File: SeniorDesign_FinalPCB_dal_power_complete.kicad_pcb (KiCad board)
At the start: 2 copper layers, 172.7 x 167.4 mm, 262 parts, among them J1 5000, J10 5000, J11 POWER, J12 AudioJack3, J2 5000, J3 5000, J4 5000, J5 5000, J6 5000, J7 5000, J8 5000, J9 5000, Q1 Si7450DP, Q10 Si7450DP, Q11 Si7450DP, Q12 Si7450DP, Q13 Si7450DP, Q14 Si7450DP, Q15 Si7450DP, Q16 Si7450DP, Q2 Si7450DP, Q3 Si7450DP, Q4 Si7450DP, Q5 Si7450DP, Q6 Si7450DP, Q7 Si7450DP, Q8 Si7450DP, Q9 Si7450DP, U1 Transducer, U10 Transducer, U11 Transducer, U12 Transducer, U13 Transducer, U14 Transducer, U15 Transducer, U16 Transducer, U17 Transducer, U18 Transducer, U19 Transducer, U2 Transducer, U20 Transducer, U21 Transducer, U22 Transducer, U23 Transducer, U24 Transducer, U25 Transducer, U26 Transducer, U27 Transducer, U28 Transducer, U29 Transducer, U3 Transducer, U30 Transducer, U31 Transducer, U32 Transducer, U33 Transducer, U34 Transducer, U35 Transducer, U36 Transducer, U37 Transducer, U38 Transducer, U39 Transducer, U4 Transducer, U40 Transducer, U41 Transducer, U42 Transducer, U43 Transducer, U44 Transducer, U45 Transducer, U46 Transducer, U47 Transducer, U48 Transducer, U49 Transducer, U5 Transducer, U50 Transducer, U51 Transducer, U52 Transducer, U53 Transducer, U54 Transducer, U55 Transducer, U56 Transducer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

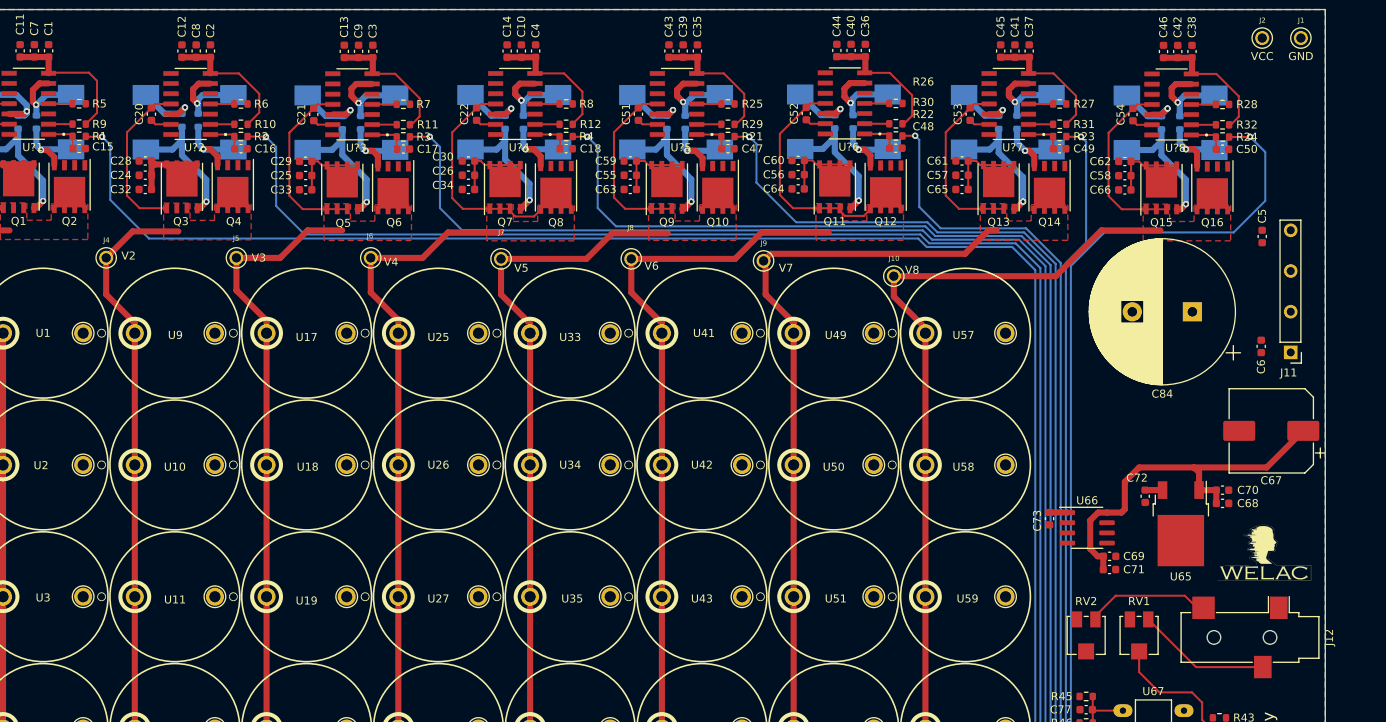
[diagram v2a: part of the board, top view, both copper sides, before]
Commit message: Add 3D Models, Adjust components, Minor changes
- Footprint for 1206 Capacitors is in the footprints folder
- Added a mostly correct size transducer 3D model
- Added the 3D model for the screw terminal
- The above models are in a new folder called SeniorDesign_3DModels
- Fixed some component placements and silkscreens that overlapped
- Added 3D models for all resistors and capacitors of the power circuits
- Fixed the VCC testpoint to be VPP
- Adjusted the Transducer footprint to be 16.3mm in diameter in the event it is deemed necessary to change the spacing of the transducers to make sure they dont interfere with each other
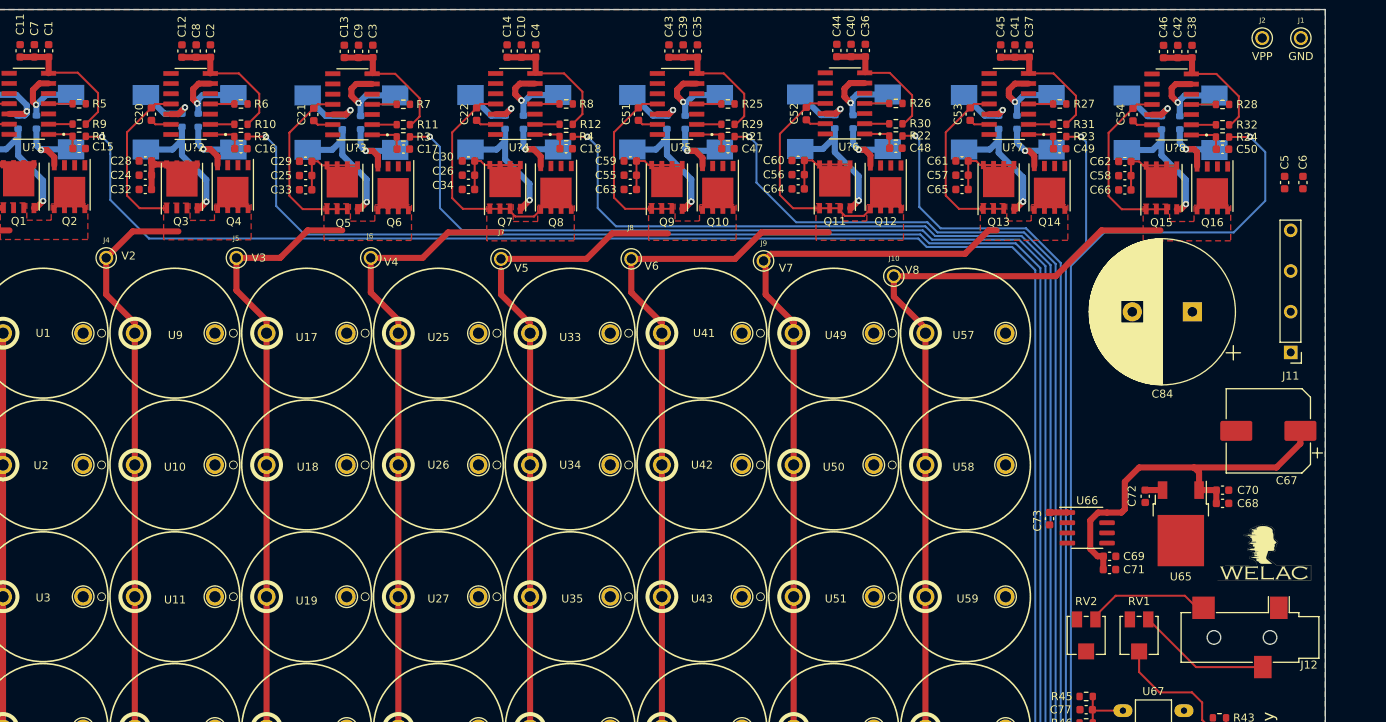
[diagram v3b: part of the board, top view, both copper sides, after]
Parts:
- moved C6 21.1 mm to (472.2, 41.4), turned to -90 degrees
- moved C5 7.29 mm to (469.9, 41.4), turned to -90 degrees
- moved C67 0.37 mm to (467.9, 72.4)
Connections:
- J2 pad 1: VCC -> VPP
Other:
- board text added: "VPP"
- board text removed: "VCC"

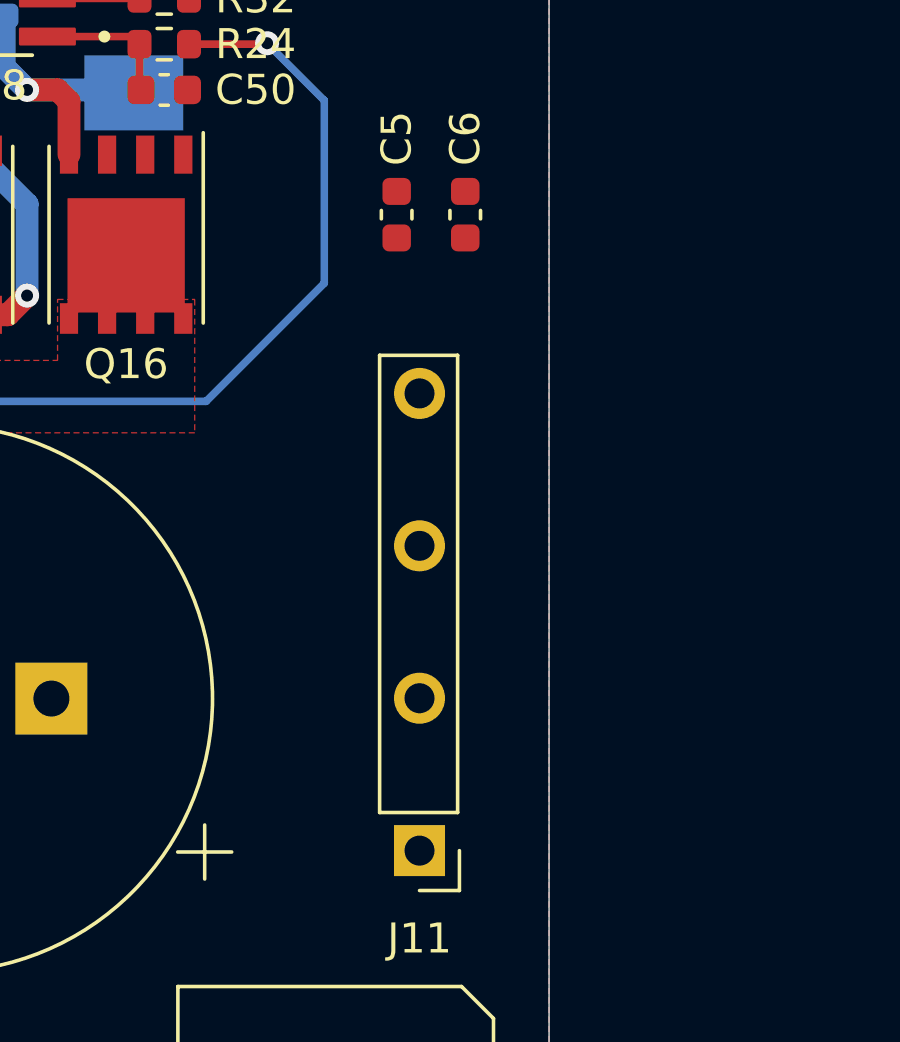
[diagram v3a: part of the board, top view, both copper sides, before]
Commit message: Add missing traces
Added traces on capacitors above the screw terminal
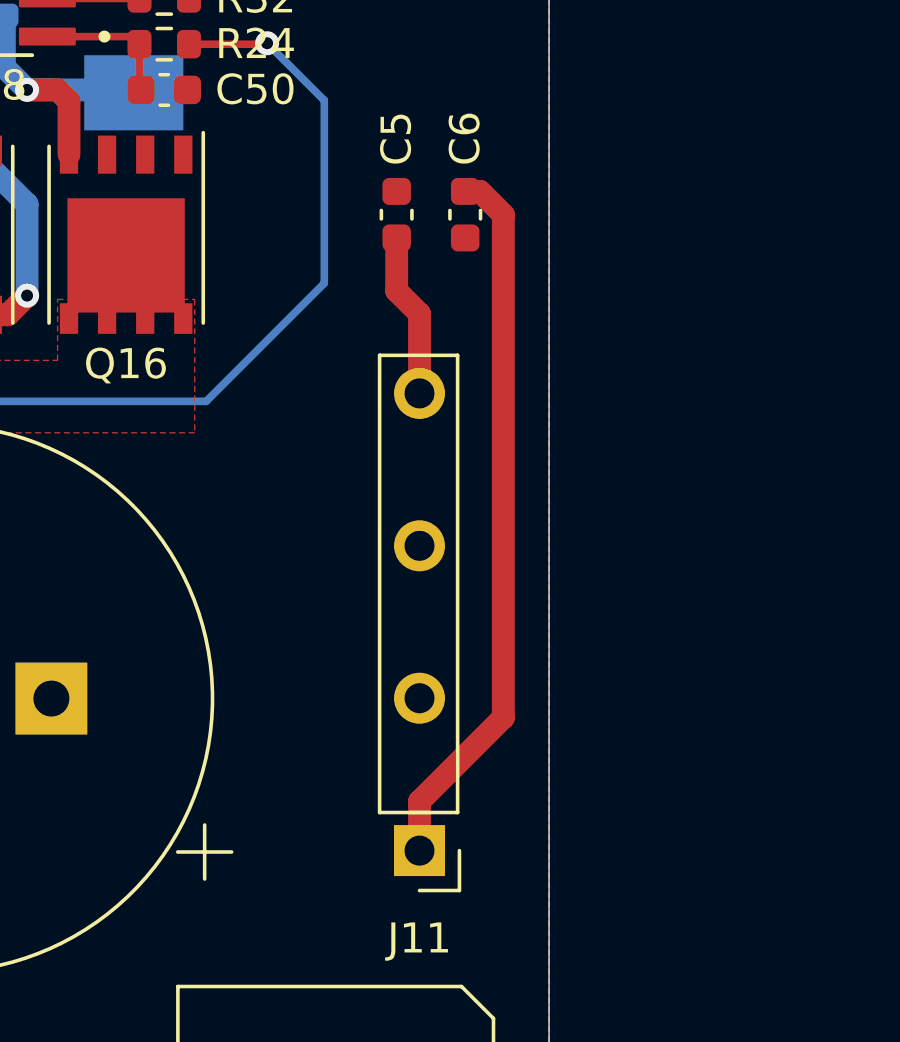
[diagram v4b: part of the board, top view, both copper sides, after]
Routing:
- net +12V: track 183.7 -> 207.6 mm
- net VPP: track 75.6 -> 81.1 mm
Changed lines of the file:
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@@
   (segment (start 396.621 27.699) (end 396.536 27.784) (width 0.25) (layer "F.Cu") (net 2))
   (segment (start 423.418 33.049) (end 423.418 30.509) (width 0.25) (layer "F.Cu") (net 2))
+  (segment (start 470.662 62.6) (end 470.662 60.96) (width 0.762) (layer "F.Cu") (net 2))
   (segment (start 420.624 27.715) (end 417.491 27.715) (width 0.25) (layer "F.Cu") (net 2))
   (segment (start 446.567 88.046) (end 445.643 87.122) (width 0.762) (layer "F.Cu") (net 2))
@@
   (segment (start 339.4005 27.784) (end 335.83 27.784) (width 0.25) (layer "F.Cu") (net 2))
   (segment (start 442.658 34.134) (end 443.865 32.927) (width 0.25) (layer "F.Cu") (net 2))
+  (segment (start 470.662 60.96) (end 473.456 58.166) (width 0.762) (layer "F.Cu") (net 2))
   (segment (start 447.738 82.585) (end 449.545 82.585) (width 0.762) (layer "F.Cu") (net 2))
   (segment (start 468.884 76.962) (end 471.868 73.978) (width 0.762) (layer "F.Cu") (net 2))
   (segment (start 471.868 73.978) (end 471.868 72.39) (width 0.762) (layer "F.Cu") (net 2))
   (segment (start 449.545 82.585) (end 449.961 82.169) (width 0.762) (layer "F.Cu") (net 2))
+  (segment (start 473.456 41.402) (end 472.681 40.627) (width 0.762) (layer "F.Cu") (net 2))
   (segment (start 446.624 82.585) (end 447.738 82.585) (width 0.762) (layer "F.Cu") (net 2))
   (segment (start 422.402 34.065) (end 423.418 33.049) (width 0.25) (layer "F.Cu") (net 2))
@@
   (segment (start 447.269 89.697) (end 447.269 88.059) (width 0.762) (layer "F.Cu") (net 2))
   (segment (start 376.428 27.699) (end 376.343 27.784) (width 0.25) (layer "F.Cu") (net 2))
+  (segment (start 473.456 58.166) (end 473.456 41.402) (width 0.762) (layer "F.Cu") (net 2))
   (segment (start 434.467 25.765) (end 438.023 25.765) (width 0.762) (layer "F.Cu") (net 2))
   (segment (start 315.6515 25.739) (end 315.6515 27.7435) (width 0.762) (layer "F.Cu") (net 2))
@@
   (segment (start 320.2865 34.108) (end 321.818 32.5765) (width 0.254) (layer "F.Cu") (net 2))
   (segment (start 445.643 83.566) (end 446.624 82.585) (width 0.762) (layer "F.Cu") (net 2))
+  (segment (start 472.681 40.627) (end 472.186 40.627) (width 0.762) (layer "F.Cu") (net 2))
   (segment (start 312.0955 25.739) (end 315.6515 25.739) (width 0.762) (layer "F.Cu") (net 2))
   (segment (start 321.818 30.226) (end 319.278 27.686) (width 0.254) (layer "F.Cu") (net 2))
@@
   (segment (start 374.523 39.213) (end 370.713 39.213) (width 0.25) (layer "F.Cu") (net 3))
   (segment (start 436.118 39.213) (end 432.308 39.213) (width 0.25) (layer "F.Cu") (net 3))
+  (segment (start 470.662 44.704) (end 469.9 43.942) (width 0.762) (layer "F.Cu") (net 3))
   (segment (start 308.115 42.346) (end 308.115 38.79) (width 0.762) (layer "F.Cu") (net 3))
   (segment (start 431.419 38.706) (end 430.416 38.706) (width 0.25) (layer "F.Cu") (net 3))
@@
   (segment (start 370.713 39.213) (end 370.077 39.213) (width 0.25) (layer "F.Cu") (net 3))
   (segment (start 328.9265 39.141) (end 328.4915 38.706) (width 0.762) (layer "F.Cu") (net 3))
+  (segment (start 469.9 43.942) (end 469.9 42.177) (width 0.762) (layer "F.Cu") (net 3))
   (segment (start 411.861 39.144) (end 411.479 39.144) (width 0.25) (layer "F.Cu") (net 3))
   (segment (start 370.077 39.213) (end 369.57 38.706) (width 0.25) (layer "F.Cu") (net 3))
@@
   (segment (start 430.416 38.706) (end 430.416 42.262) (width 0.25) (layer "F.Cu") (net 3))
   (segment (start 390.017 38.706) (end 389.014 38.706) (width 0.25) (layer "F.Cu") (net 3))
+  (segment (start 470.662 47.36) (end 470.662 44.704) (width 0.762) (layer "F.Cu") (net 3))
   (segment (start 369.57 38.706) (end 368.821 38.706) (width 0.25) (layer "F.Cu") (net 3))
   (segment (start 409.969 38.637) (end 409.969 42.193) (width 0.25) (layer "F.Cu") (net 3))
